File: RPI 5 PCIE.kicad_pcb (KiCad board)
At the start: 2 copper layers, 6 parts, among them J1 Conn_01x16, J2 ATX-24, Q1 MMBT3904

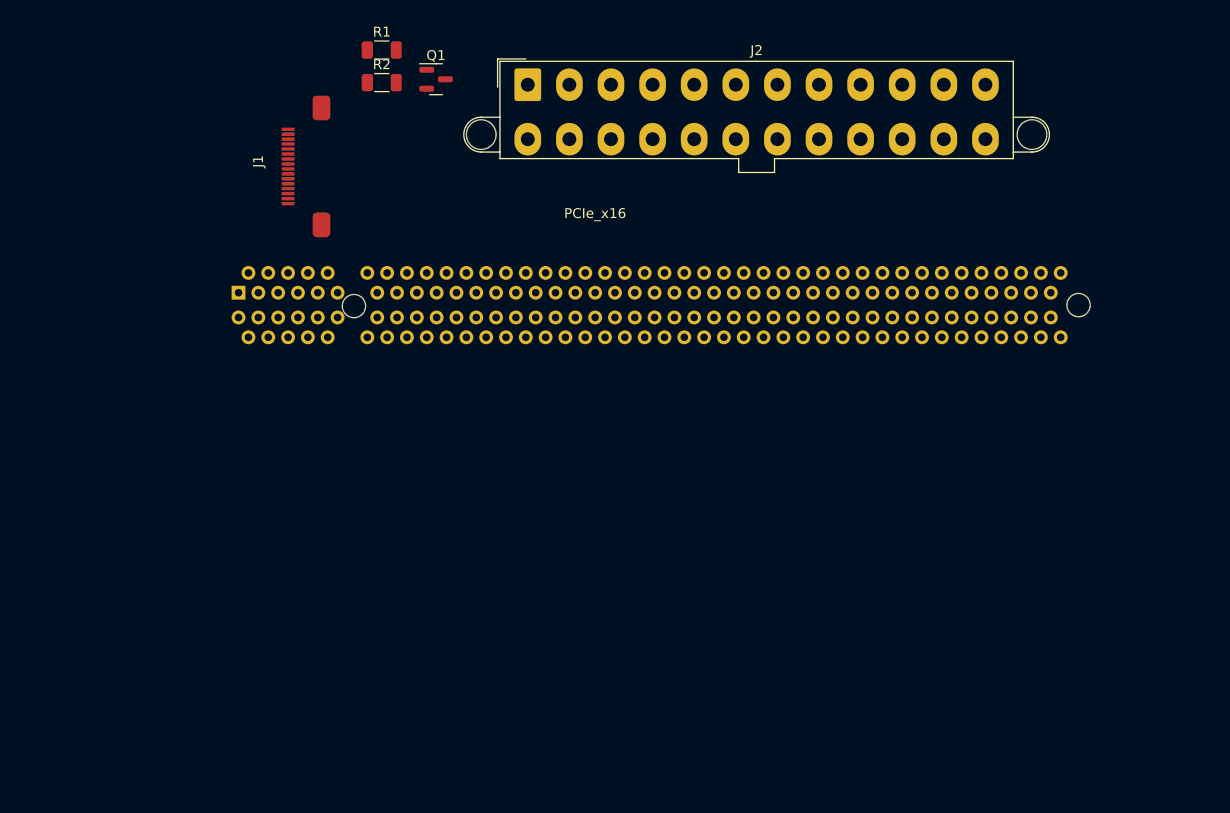
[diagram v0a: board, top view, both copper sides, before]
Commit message: Attempted PCB Design
Realized that a 4-layer PCB is required. Will continue research into impedance controlled PCBs
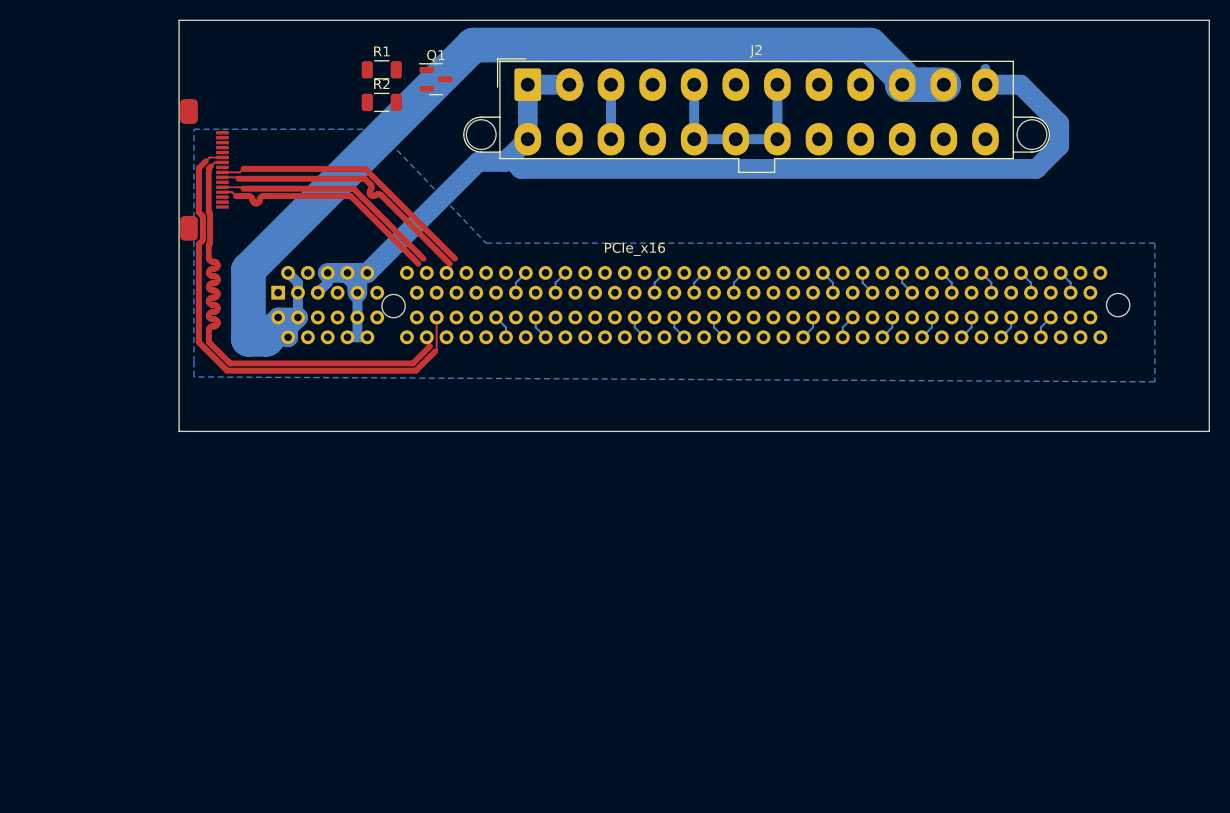
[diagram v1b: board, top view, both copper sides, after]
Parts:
- moved J1 6.63 mm to (120.4, 62.1), turned to -90 degrees
- moved PCIe_x16 4.00 mm to (126.0, 75.8)
- moved R1 2.00 mm to (136.5, 52.0)
- moved R2 2.00 mm to (136.5, 55.3)
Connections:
- net Net-(J1-Pin_10) renamed /PCIE_TX_P
- net Net-(J1-Pin_11) renamed /PCIE_TX_N
- net Net-(J1-Pin_15) renamed /PCIE_CLKREQ_N
- net Net-(J1-Pin_16) renamed /PCIE_RST_B
- net Net-(J1-Pin_4) renamed /PCIE_CLK_P
- net Net-(J1-Pin_5) renamed /PCIE_CLK_N
- net Net-(J1-Pin_7) renamed /PCIE_RX_P
- net Net-(J1-Pin_8) renamed /PCIE_RX_N
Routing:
- net +3.3V: track 0.00 -> 119.1 mm
- net +12V: track 0.00 -> 105.4 mm
- net GND: track 0.00 -> 82.8 mm
- net /PCIE_TX_P: track 0.00 -> 50.2 mm
- net /PCIE_TX_N: track 0.00 -> 50.1 mm
- net /PCIE_RX_P: track 0.00 -> 27.4 mm
- net /PCIE_RX_N: track 0.00 -> 27.4 mm
- net /PCIE_CLK_P: track 0.00 -> 23.6 mm
- net /PCIE_CLK_N: track 0.00 -> 23.3 mm
- added copper zone on B.Cu, net GND
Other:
- board outline added: 104 x 41.5 mm

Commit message: Updated PCB to 4-layer Board
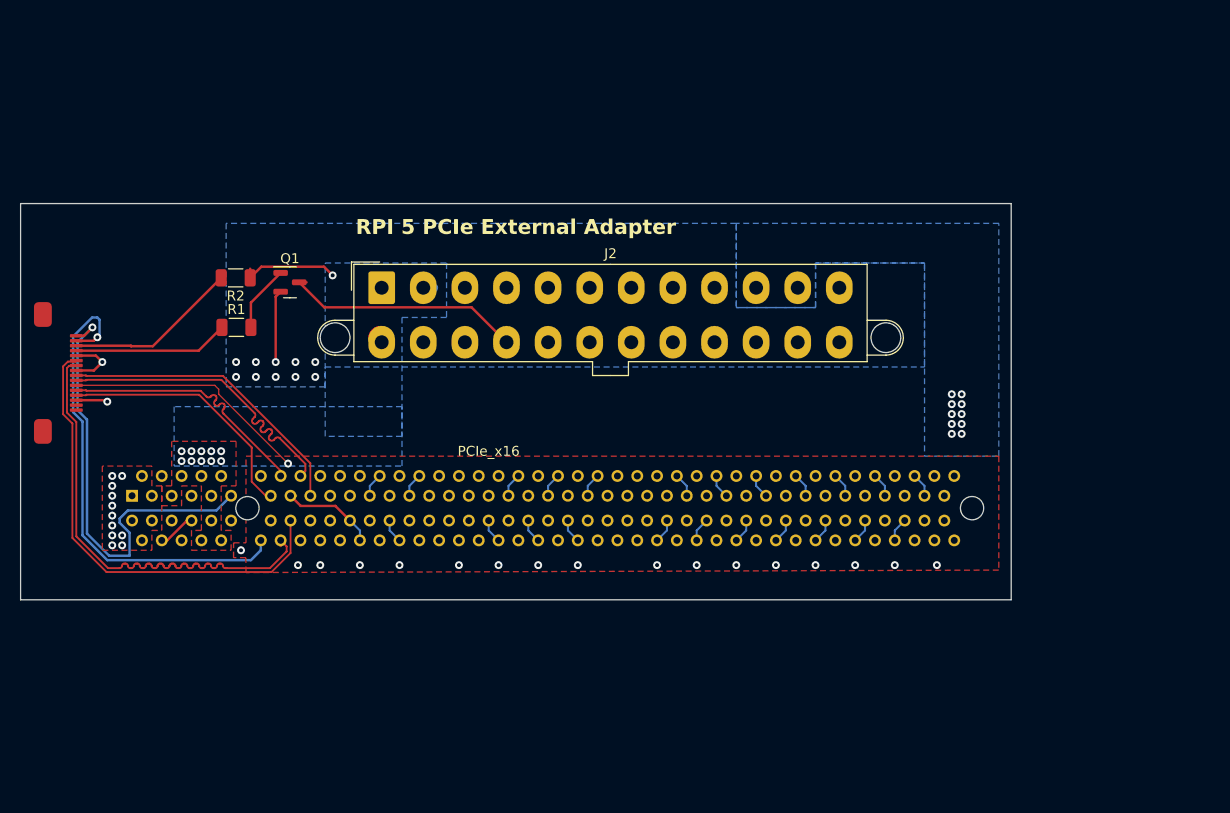
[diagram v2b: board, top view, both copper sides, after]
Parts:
- moved R1 29.9 mm to (121.8, 78.0)
- moved J2 25.3 mm to (136.4, 74.0)
- moved PCIe_x16 25.3 mm to (111.2, 96.2)
- moved Q1 25.3 mm to (127.2, 73.5)
- moved J1 25.3 mm to (105.6, 82.6)
- moved R2 23.0 mm to (121.7, 73.0), turned to 180 degrees
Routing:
- net +3.3V: track 119.1 -> 11.6 mm, vias 0 -> 11
- net +12V: track 105.4 -> 0.00 mm, vias 0 -> 21
- net /PCIE_CLKREQ_N: track 0.00 -> 48.6 mm, vias 0 -> 1
- net /PCIE_RST_B: track 0.00 -> 45.4 mm, vias 0 -> 1
- net GND: track 82.8 -> 111.1 mm, vias 0 -> 30
- net Net-(J2-PS_ON#): track 0.00 -> 24.2 mm
- net Net-(J1-Pin_14): track 0.00 -> 17.5 mm
- net Net-(J1-Pin_13): track 0.00 -> 15.7 mm
- net Net-(Q1-B): track 0.00 -> 6.74 mm
- net /PCIE_RX_P: track 27.4 -> 31.4 mm
- net /PCIE_TX_N: track 50.1 -> 46.8 mm
- net /PCIE_RX_N: track 27.4 -> 30.6 mm
- net /PCIE_CLK_N: track 23.3 -> 26.2 mm
- net /PCIE_CLK_P: track 23.6 -> 25.9 mm
- net /PCIE_TX_P: track 50.2 -> 48.4 mm
- added copper zone on B.Cu, net +12V
- added copper zone on F.Cu, net +12V
- added copper zone on In2.Cu, net +12V
- added copper zone on B.Cu, net +3.3V
- added copper zone on F.Cu, net +3.3V
- added copper zone on F.Cu, net GND
- added copper zone on In1.Cu, net GND
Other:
- board size 104 x 41.5 mm -> 100 x 40 mm
- copper layers 2 -> 4
- board text added: "RPI 5 PCIe External Adapter"

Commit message: Small PCB updates
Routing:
- net +3.3V: track 11.6 -> 55.5 mm
- net unconnected-(J2-+5V-Pad21): track 0.00 -> 33.4 mm
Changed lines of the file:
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@@
   (segment (start 107.975 77.225) (end 107.75 77) (width 0.25) (layer "B.Cu") (net 12))
   (segment (start 105.3 86.55) (end 106.25 87.5) (width 0.25) (layer "B.Cu") (net 12))
+  (segment (start 180.373 71.723) (end 142.927 71.723) (width 1) (layer "F.Cu") (net 13))
   (segment (start 123.175 73) (end 124.3 71.875) (width 0.25) (layer "F.Cu") (net 13))
   (segment (start 123.175 73) (end 123.175 72.075) (width 0.25) (layer "F.Cu") (net 13))
   (segment (start 136.35 79.1) (end 136.45 79.1) (width 2.5) (layer "F.Cu") (net 13))
+  (segment (start 142.927 71.723) (end 140.65 74) (width 1) (layer "F.Cu") (net 13))
   (segment (start 130.625 71.875) (end 131.5 72.75) (width 0.25) (layer "F.Cu") (net 13))
   (segment (start 124.3 71.875) (end 130.625 71.875) (width 0.25) (layer "F.Cu") (net 13))
   (segment (start 136.45 79.5) (end 136.45 79.2) (width 2.5) (layer "F.Cu") (net 13))
   (segment (start 136.45 79.2) (end 136.35 79.1) (width 2.5) (layer "F.Cu") (net 13))
+  (segment (start 182.65 74) (end 180.373 71.723) (width 1) (layer "F.Cu") (net 13))
   (via (at 120.25 90.5) (size 0.8) (drill 0.4) (layers "F.Cu" "B.Cu") (free) (net 13))
   (via (at 119.25 91.5) (size 0.8) (drill 0.4) (layers "F.Cu" "B.Cu") (free) (net 13))
@@
   (via (at 116.25 91.5) (size 0.8) (drill 0.4) (layers "F.Cu" "B.Cu") (free) (net 13))
   (segment (start 141.650862 74) (end 140.65 74) (width 1) (layer "B.Cu") (net 13))
+  (segment (start 155.423 76.027) (end 157.45 74) (width 0.5) (layer "F.Cu") (net 14))
+  (segment (start 149.05 74) (end 151.077 76.027) (width 0.5) (layer "F.Cu") (net 14))
+  (segment (start 174.25 79.5) (end 170.05 79.5) (width 0.5) (layer "F.Cu") (net 14))
+  (segment (start 151.077 76.027) (end 155.423 76.027) (width 0.5) (layer "F.Cu") (net 14))
+  (segment (start 170.05 79.5) (end 168.023 77.473) (width 0.5) (layer "F.Cu") (net 14))
+  (segment (start 168.023 77.473) (end 160.923 77.473) (width 0.5) (layer "F.Cu") (net 14))
+  (segment (start 178.45 79.5) (end 174.25 79.5) (width 0.5) (layer "F.Cu") (net 14))
+  (segment (start 157.45 74) (end 160.923 77.473) (width 0.5) (layer "F.Cu") (net 14))
   (via (at 194 85.75) (size 0.8) (drill 0.4) (layers "F.Cu" "B.Cu") (free) (net 17))
   (via (at 195 86.75) (size 0.8) (drill 0.4) (layers "F.Cu" "B.Cu") (free) (net 17))
@@
     (polygon
       (pts
-        (xy 118.5 51)
-        (xy 118.5 86)
-        (xy 215.5 85.75)
-        (xy 215.5 50.75)
+        (xy 102.53164 69.276336)
+        (xy 102.53164 104.276336)
+        (xy 199.53164 104.026336)
+        (xy 199.53164 69.026336)
       )
     )
@@
         (xy 180.25 76)
         (xy 172.25 76)
-        (xy 172.25 67.5)
-        (xy 120.75 67.5)
+        (xy 172.25 65.75)
+        (xy 121 65.75)
       )
     )
@@
         (xy 191.25 91)
         (xy 198.75 91)
-        (xy 198.75 67.5)
-        (xy 172.25 67.5)
-      )
-    )
+        (xy 198.75 65.75)
+        (xy 172.25 65.75)
+      )
+    )

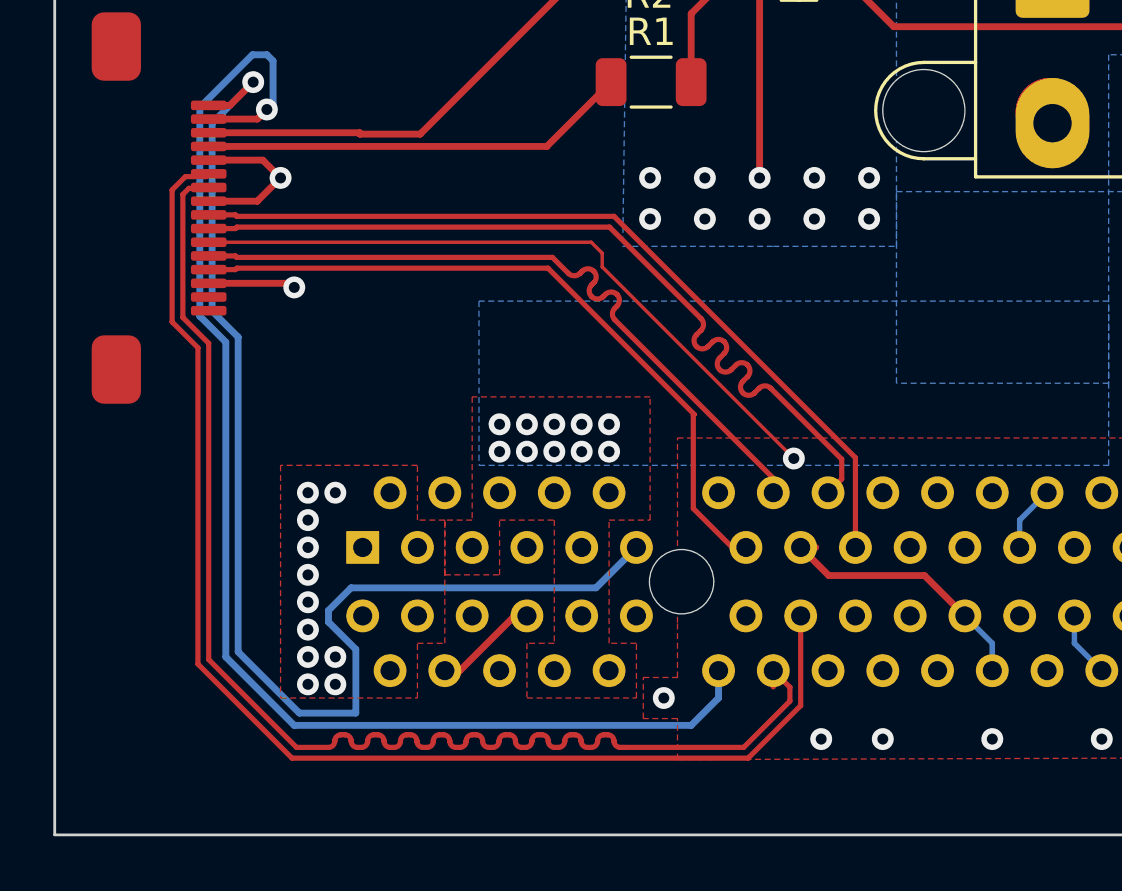
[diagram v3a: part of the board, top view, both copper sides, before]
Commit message: Updated Tracer Width to JLCPCB recommendations
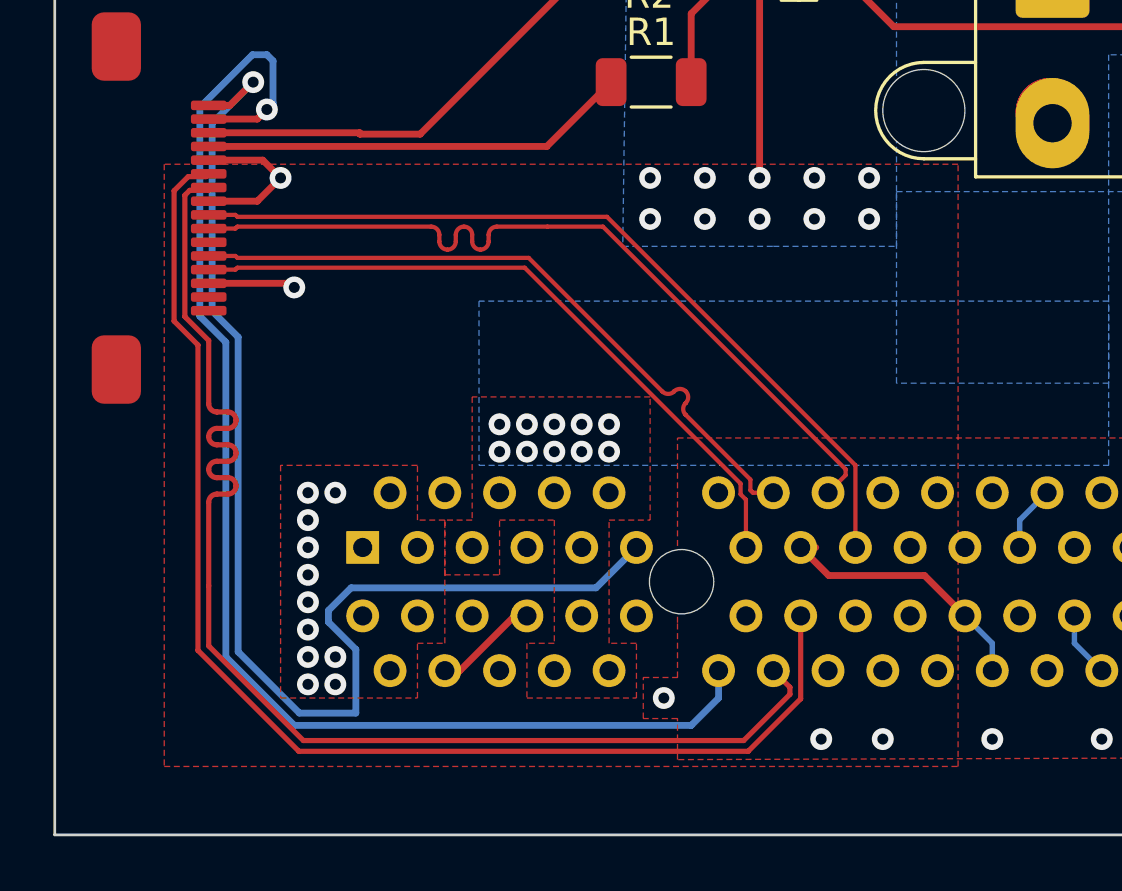
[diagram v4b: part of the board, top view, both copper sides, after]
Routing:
- net GND: track 111.1 -> 86.2 mm, vias 30 -> 29
- net /PCIE_TX_P: track 48.4 -> 47.1 mm
- net /PCIE_CLK_N: track 26.2 -> 25.1 mm
- net /PCIE_RX_P: track 31.4 -> 30.3 mm
- net /PCIE_TX_N: track 46.8 -> 46.0 mm

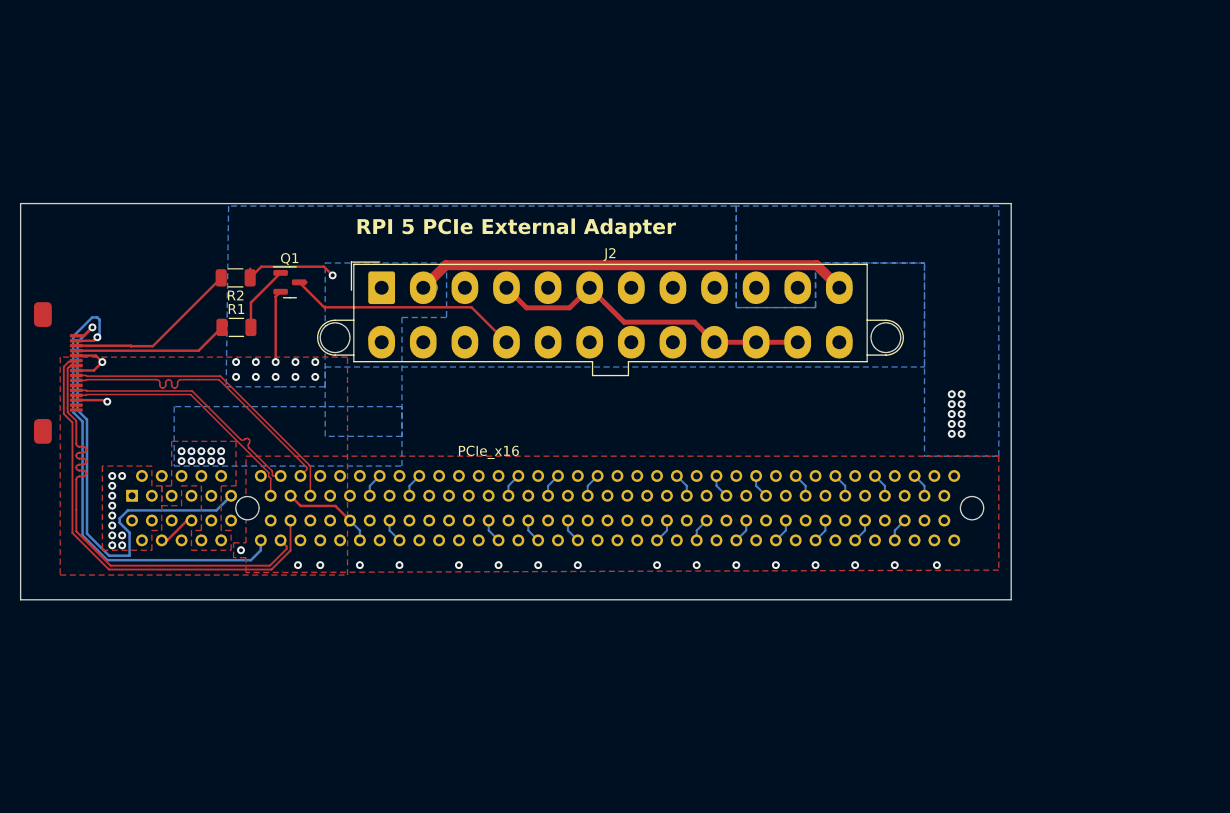
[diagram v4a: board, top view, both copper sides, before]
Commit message: Finished PCB v1
This was the first prototype to be sent to JLC PCB
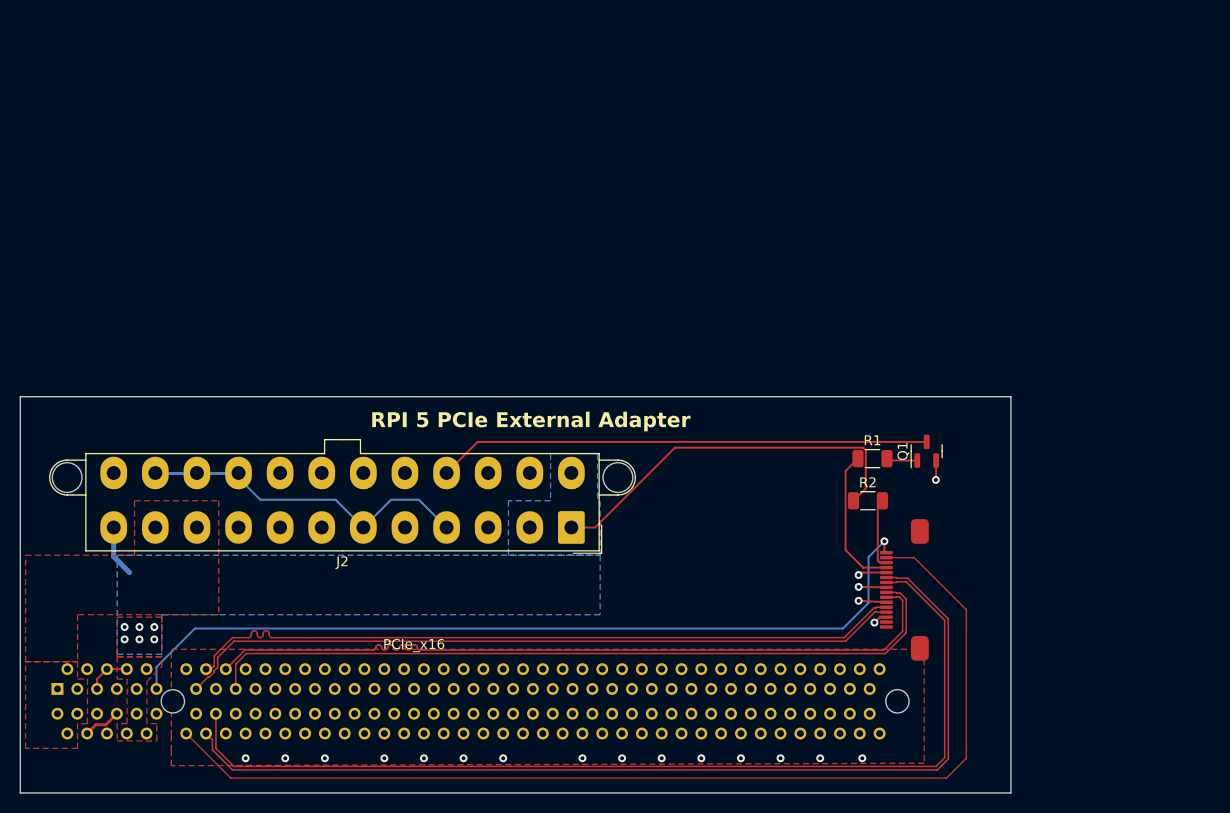
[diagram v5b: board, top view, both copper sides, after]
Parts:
- moved J1 84.7 mm to (187.4, 104.5), turned to 90 degrees
- moved R2 67.7 mm to (185.5, 95.5), turned to 0 degrees
- moved Q1 66.5 mm to (191.5, 90.5), turned to 90 degrees
- moved R1 65.6 mm to (186.0, 91.2)
- moved J2 30.9 mm to (155.6, 98.2), turned to 180 degrees
- moved PCIe_x16 20.9 mm to (103.7, 115.8)
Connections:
- J1 pad 10: /PCIE_TX_P -> /PCIE_TX_N
- J1 pad 11: /PCIE_TX_N -> /PCIE_TX_P
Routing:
- net GND: track 86.2 -> 16.3 mm, vias 29 -> 20
- net /PCIE_CLKREQ_N: track 48.6 -> 106.7 mm, vias 1 -> 0
- net /PCIE_TX_N: track 46.0 -> 99.6 mm
- net /PCIE_TX_P: track 47.1 -> 100.0 mm
- net /PCIE_CLK_P: track 25.6 -> 74.1 mm
- net /PCIE_CLK_N: track 25.1 -> 73.6 mm
- net /PCIE_RX_N: track 30.4 -> 77.2 mm
- net /PCIE_RX_P: track 30.3 -> 77.0 mm
- net /PCIE_RST_B: track 45.4 -> 84.9 mm
- net Net-(J2-PS_ON#): track 24.2 -> 49.8 mm
- net Net-(J1-Pin_14): track 17.5 -> 7.19 mm
- net +3.3V: track 55.5 -> 48.4 mm, vias 11 -> 6
- net Net-(Q1-B): track 6.74 -> 3.13 mm
- net unconnected-(J2-+5V-Pad21): track 33.4 -> 34.3 mm
- net +12V: vias 21 -> 0
- removed copper zone on B.Cu, net +12V
- removed copper zone on In2.Cu, net +12V
- removed copper zone on B.Cu, net GND
